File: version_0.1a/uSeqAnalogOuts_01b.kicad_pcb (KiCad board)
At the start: 2 copper layers, 23.4 x 110 mm, 130 parts, among them J1 Out A1, J11 Conn_01x04, J2 Out A2, J3 Out A3, J4 Out A4, J5 Out A5, J6 Out A7, J7 Out A6, J8 Out A8, J9 Conn_01x20, U1 TL072, U2 CJ431 SOT-23, U3 CJ431 SOT-23, U4 TL072, U5 CJ431 SOT-23, U6 CJ431 SOT-23, U7 TL072, U8 TL072

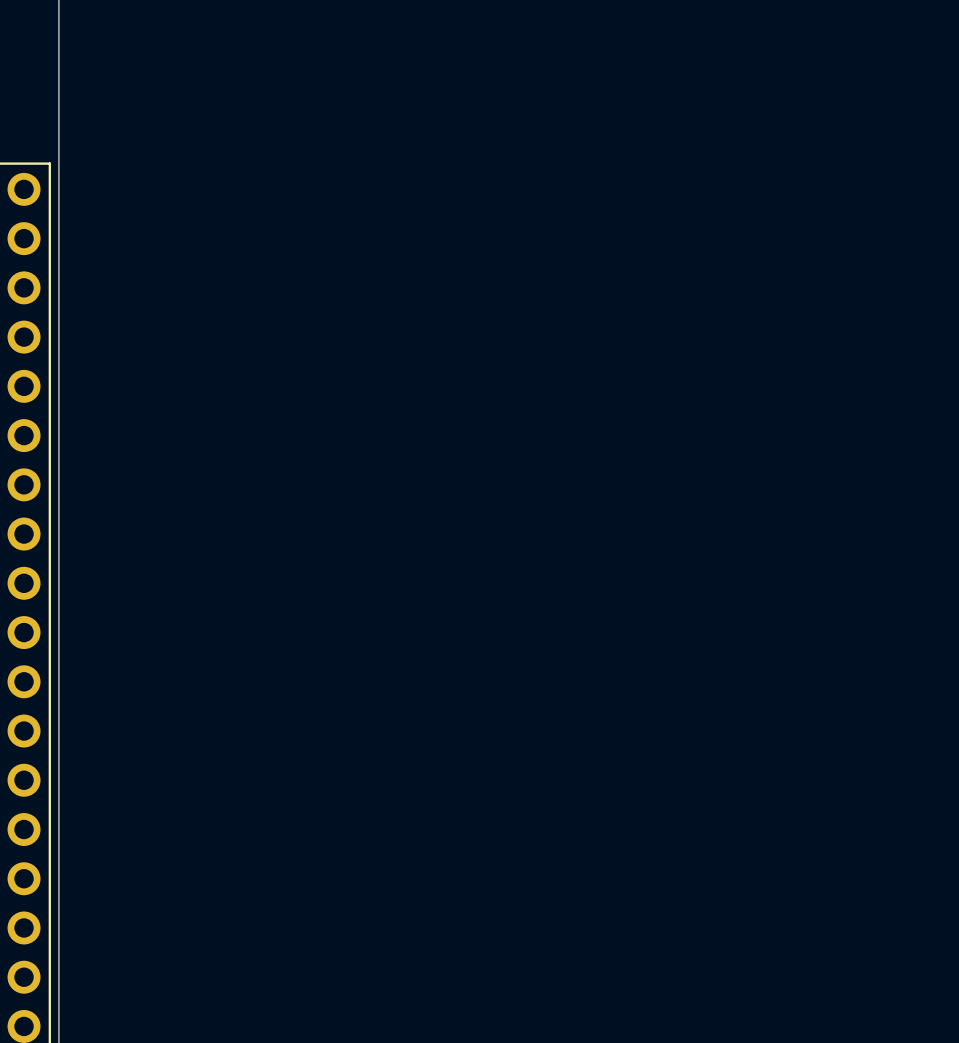
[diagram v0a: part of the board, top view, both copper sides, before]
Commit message: Added version 0.1a
0.1a uses hierachical schematic and replicate layout plugin to copy a pair of channels 4 times
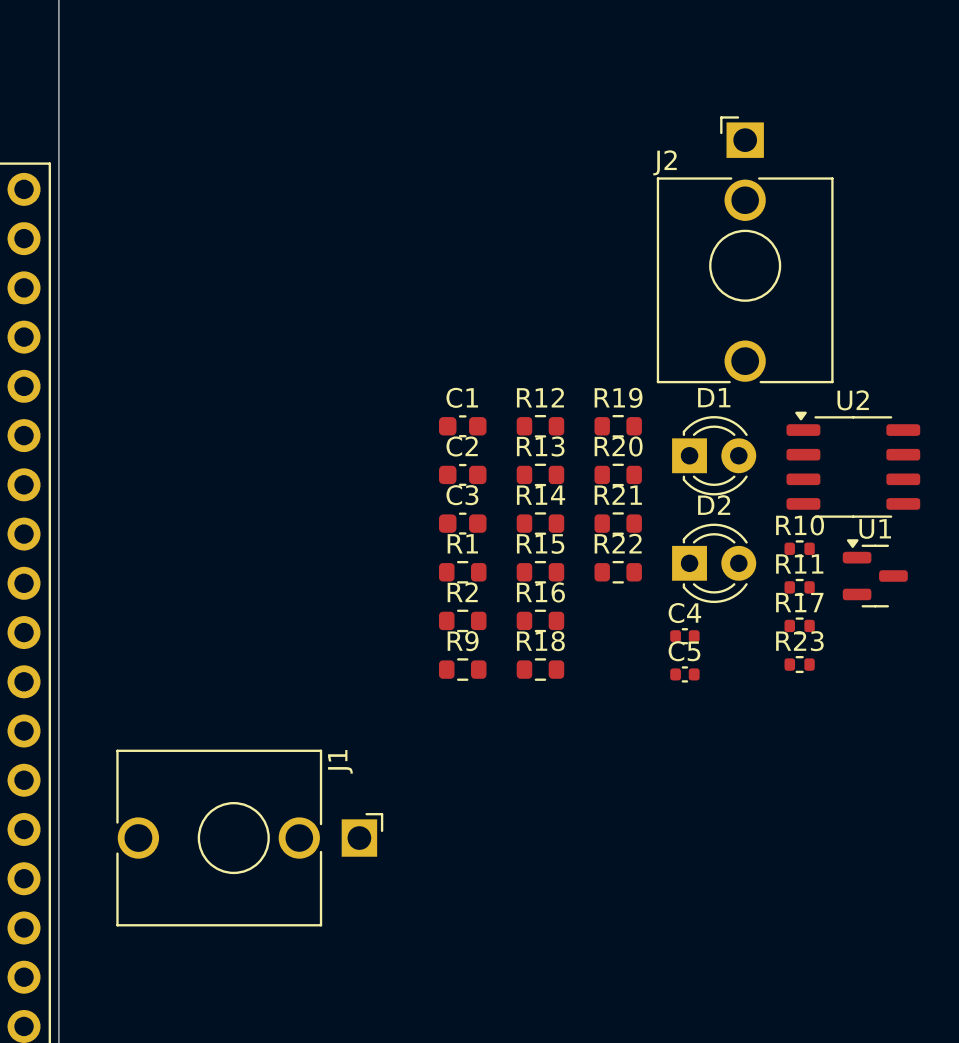
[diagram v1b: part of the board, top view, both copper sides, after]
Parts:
- added C1: 10u, Capacitor_SMD:C_0603_1608Metric, F.Cu at (195.2, 123.0)
- added C2: 100n, Capacitor_SMD:C_0603_1608Metric, F.Cu at (195.2, 125.5)
- added C3: 100n, Capacitor_SMD:C_0603_1608Metric, F.Cu at (195.2, 128.0)
- added C4: 10n, Capacitor_SMD:C_0402_1005Metric, F.Cu at (206.7, 133.8)
- added C5: 10n, Capacitor_SMD:C_0402_1005Metric, F.Cu at (206.7, 135.8)
- added D1: LED A4, LED_THT:LED_D3.0mm_FlatTop, F.Cu at (206.9, 124.5)
- added D2: LED A5, LED_THT:LED_D3.0mm_FlatTop, F.Cu at (206.9, 130.0)
- added J1: Out A5, Connector_Audio:Jack_3.5mm_QingPu_WQP-PJ398SM_Vertical_CircularHoles, F.Cu at (189.9, 144.2)
- added J2: Out A6, Connector_Audio:Jack_3.5mm_QingPu_WQP-PJ398SM_Vertical_CircularHoles, F.Cu at (209.8, 108.2)
- added R1: 9.1k, Resistor_SMD:R_0603_1608Metric, F.Cu at (195.2, 130.5)
- added R10: 5.1k 1%, Resistor_SMD:R_0402_1005Metric, F.Cu at (212.6, 129.3)
- added R11: 5.1k 1%, Resistor_SMD:R_0402_1005Metric, F.Cu at (212.6, 131.3)
- added R12: 12k, Resistor_SMD:R_0603_1608Metric, F.Cu at (199.2, 123.0)
- added R13: 10k, Resistor_SMD:R_0603_1608Metric, F.Cu at (199.2, 125.5)
- added R14: 33k, Resistor_SMD:R_0603_1608Metric, F.Cu at (199.2, 128.0)
- added R15: 47k, Resistor_SMD:R_0603_1608Metric, F.Cu at (199.2, 130.5)
- added R16: 47k, Resistor_SMD:R_0603_1608Metric, F.Cu at (199.2, 133.0)
- added R17: 1k, Resistor_SMD:R_0402_1005Metric, F.Cu at (212.6, 133.3)
- added R18: 12k, Resistor_SMD:R_0603_1608Metric, F.Cu at (199.2, 135.5)
- added R19: 10k, Resistor_SMD:R_0603_1608Metric, F.Cu at (203.2, 123.0)
- added R2: 9.1k, Resistor_SMD:R_0603_1608Metric, F.Cu at (195.2, 133.0)
- added R20: 33k, Resistor_SMD:R_0603_1608Metric, F.Cu at (203.2, 125.5)
- added R21: 47k, Resistor_SMD:R_0603_1608Metric, F.Cu at (203.2, 128.0)
- added R22: 47k, Resistor_SMD:R_0603_1608Metric, F.Cu at (203.2, 130.5)
- added R23: 1k, Resistor_SMD:R_0402_1005Metric, F.Cu at (212.6, 135.2)
- added R9: 1.8, >24mW, Resistor_SMD:R_0603_1608Metric, F.Cu at (195.2, 135.5)
- added U1: CJ431 SOT-23, Package_TO_SOT_SMD:SOT-23, F.Cu at (216.5, 130.7)
- added U2: TL072, Package_SO:SO-8_3.9x4.9mm_P1.27mm, F.Cu at (215.4, 125.1)
